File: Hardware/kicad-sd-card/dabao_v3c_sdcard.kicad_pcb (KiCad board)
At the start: 2 copper layers, 21 x 67.5 mm, 45 parts, among them J1 USB_A, J2 Micro_SD_Card, SW1 SW_Push, U1 EMS4000RSW, U2 baochip1x, U3 MT3406, U4 MT3406, U5 CM1624, Y1 48.000MHz

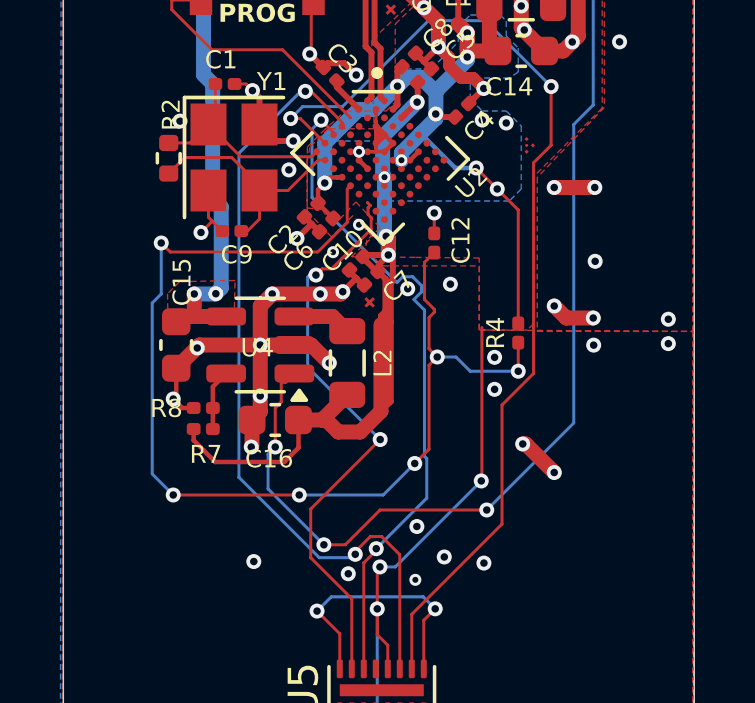
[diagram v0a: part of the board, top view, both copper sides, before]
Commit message: Hardware: add kicad-files-usb (no-SD dabao_v3c), refresh kicad-sd-card exports
Add USB-only KiCad tree under kicad-files-usb with .gitignore excluding
backups and fp-info-cache. Update kicad-sd-card PCB, PDF, previews, and gerbers.

Made-with: Cursor
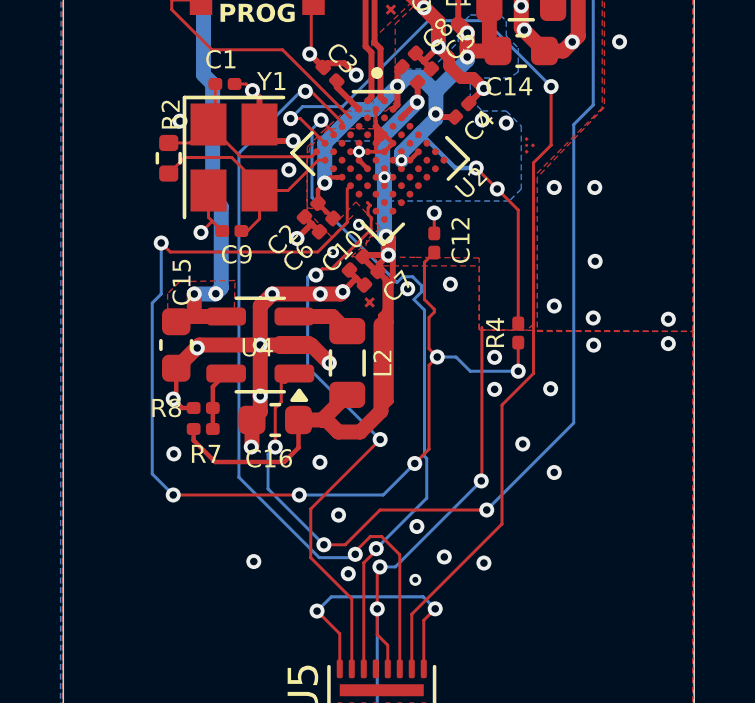
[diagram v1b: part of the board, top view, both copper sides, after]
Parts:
- removed G***: LOGO, LOGO
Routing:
- net GND: track 72.1 -> 67.8 mm, vias 85 -> 89
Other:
- board text removed: "0"
- board text removed: "0 mm"
- board text removed: "0.01 mm"
- board text removed: "0.02"
- board text removed: "0.035 mm"
- board text removed: "0.1000 mm / 0.1000 mm"
- board text removed: "0.2000 mm"
- board text removed: "1"
- board text removed: "1.52mm"
- board text removed: "1.6mm"
- board text removed: "2"
- board text removed: "21.0000 mm x 41.0000 mm"
- board text removed: "3.3"
- board text removed: "4.5"
- board text removed: "B.Cu"
- board text removed: "B.Mask"
- board text removed: "B.Paste"
- board text removed: "B.Silkscreen"
- board text removed: "BOARD CHARACTERISTICS"
- board text removed: "Board Thickness:"
- board text removed: "Board overall dimensions:"
- board text removed: "Bottom Silk Screen"
- board text removed: "Bottom Solder Mask"
- board text removed: "Bottom Solder Paste"
- board text removed: "Castellated pads:"
- board text removed: "Color"
- board text removed: "Copper Finish:"
- board text removed: "Copper Layer Count:"
- board text removed: "Dielectric 1"
- board text removed: "ENIG"
- board text removed: "Edge card connectors:"
- board text removed: "Epsilon R"
- board text removed: "F.Cu"
- board text removed: "F.Mask"
- board text removed: "F.Paste"
- board text removed: "F.Silkscreen"
- board text removed: "FR4"
- board text removed: "Green"
- board text removed: "Impedance Control:"
- board text removed: "Layer Name"
- board text removed: "Loss Tangent"
- board text removed: "Material"
- board text removed: "Min hole diameter:"
- board text removed: "Min track/spacing:"
- board text removed: "No"
- board text removed: "Not specified"
- board text removed: "Plated Board Edge:"
- board text removed: "Thickness (mm)"
- board text removed: "Top Silk Screen"
- board text removed: "Top Solder Mask"
- board text removed: "Top Solder Paste"
- board text removed: "Type"
- board text removed: "White"
- board text removed: "Yes"
- board text removed: "bunnie"
- board text removed: "copper"
- board text removed: "core"
- board text removed: "v3e 02/26"
